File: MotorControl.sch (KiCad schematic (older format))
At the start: 3 parts, among them U4 74LVC125

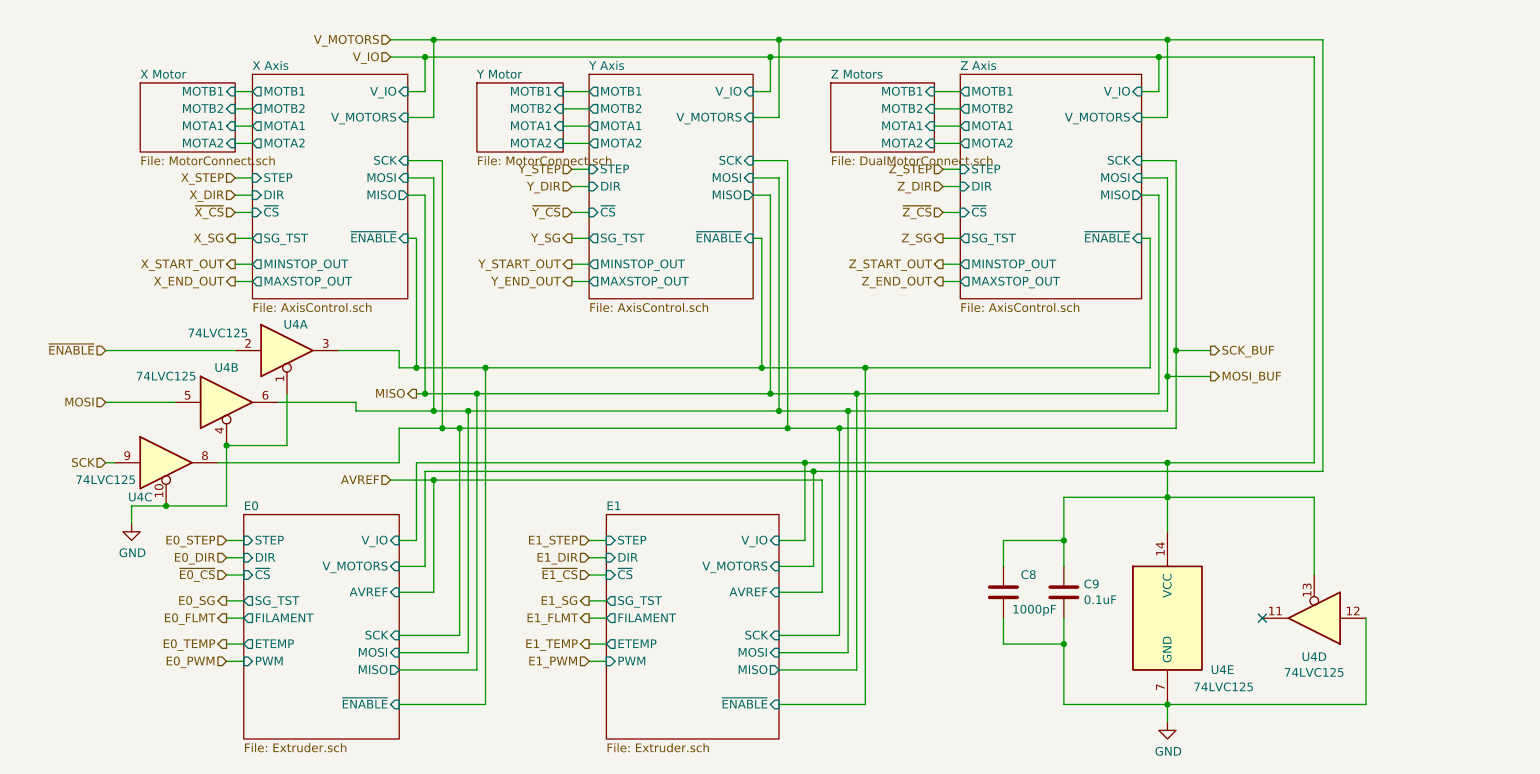
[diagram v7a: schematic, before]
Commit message: Added clock source for the TMC2660 drivers.
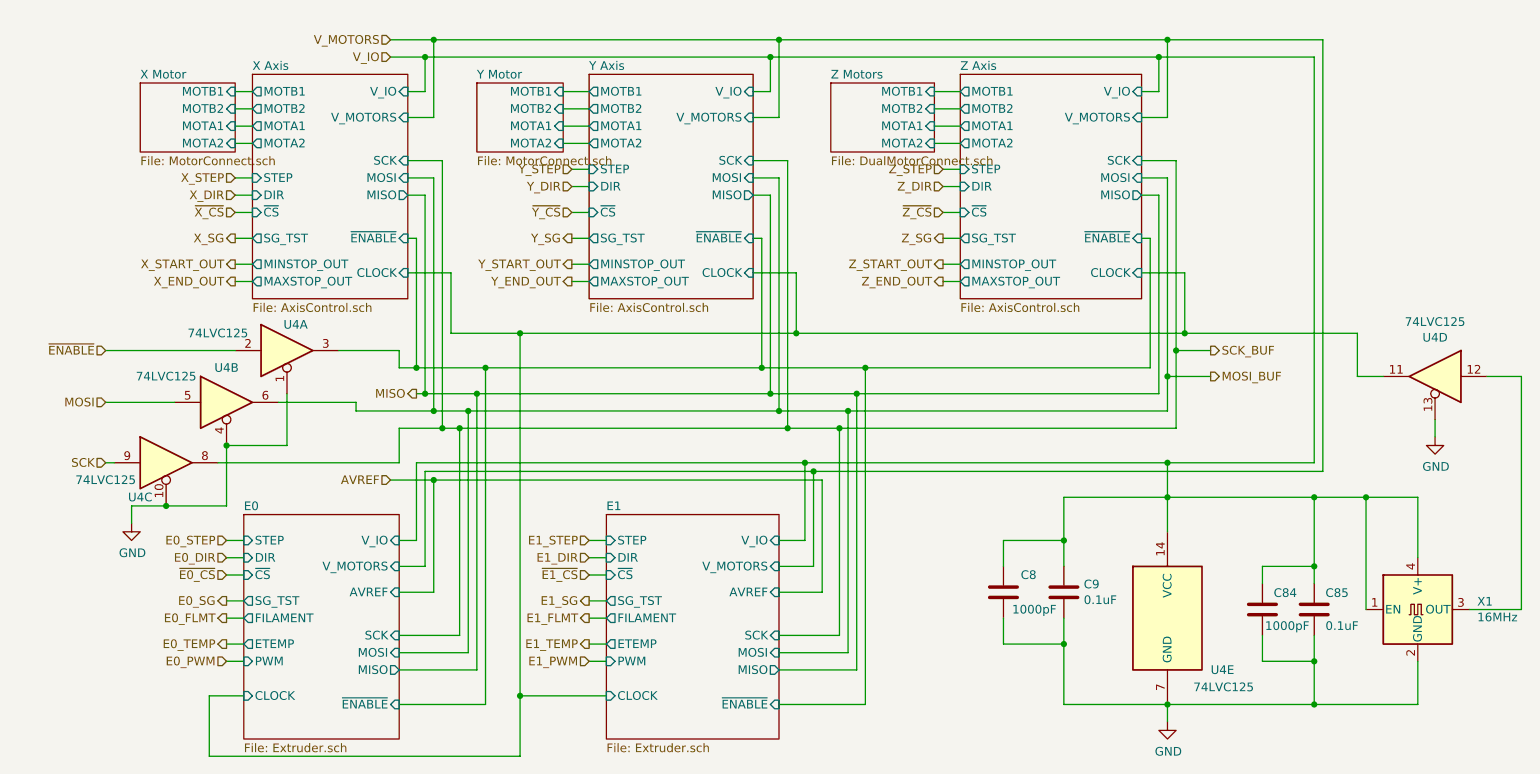
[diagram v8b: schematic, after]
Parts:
- added C84: 1000pF, PrntrBoardV1:C_0603_1608Metric, symbol Device:C
- added C85: 0.1uF, PrntrBoardV1:C_0603_1608Metric, symbol Device:C
- added X1: 16MHz, PrntrBoardV1:Oscillator_SMD_EuroQuartz_XO32-4Pin_3.2x2.5mm_HandSoldering, symbol Oscillator:XO32
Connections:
- net GND: now also U4.13, C84.2, C85.2, X1.2 (GND); no longer U4.12
- net V_IO: now also C84.1, C85.1, X1.1 (EN), X1.4 (V+); no longer U4.13
- net E0/CLOCK: now reaches U4.11
- new net: U4.12, X1.3 (OUT)
- no-connect marks 1 -> 0
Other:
- moved on the sheet: U4D
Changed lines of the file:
@@
 F14 "ETEMP" O L 3350 4600 50
 F15 "PWM" I L 3350 4700 50
+F16 "CLOCK" I L 3350 4900 50
 $EndSheet
 $Sheet
@@
 F16 "MOTA2" O L 3400 1700 50
 F17 "MOTB2" O L 3400 1500 50
+F18 "CLOCK" I R 4300 2450 50
 $EndSheet
 $Sheet
@@
 F16 "MOTA2" O L 5350 1700 50
 F17 "MOTB2" O L 5350 1500 50
+F18 "CLOCK" I R 6300 2450 50
 $EndSheet
 Wire Wire Line
@@
 F16 "MOTA2" O L 7500 1700 50
 F17 "MOTB2" O L 7500 1500 50
+F18 "CLOCK" I R 8550 2450 50
 $EndSheet
 Wire Wire Line
@@
 F14 "ETEMP" O L 5450 4600 50
 F15 "PWM" I L 5450 4700 50
+F16 "CLOCK" I L 5450 4900 50
 $EndSheet
 $Comp
 L 74ls125:74LVC125 U4
 U 4 1 5C47A3BD
-P 9550 4450
-F 0 "U4" H 9550 4675 50  0000 C CNN
-F 1 "74LVC125" H 9550 4766 50  0000 C CNN
-F 2 "Package_SO:TSSOP-14_4.4x5mm_P0.65mm" H 9550 4450 50  0001 C CNN
-F 3 "http://www.ti.com/lit/gpn/sn74LVC125" H 9550 4450 50  0001 C CNN
-	4    9550 4450
-	-1   0    0    1
-$EndComp
-Wire Wire Line
-	9850 4450 9850 4950
-Wire Wire Line
-	9850 4950 8700 4950
-Wire Wire Line
-	9550 4200 9550 3750
+P 10250 3050
+F 0 "U4" H 10250 3275 50  0000 C CNN
+F 1 "74LVC125" H 10250 3366 50  0000 C CNN
+F 2 "Package_SO:TSSOP-14_4.4x5mm_P0.65mm" H 10250 3050 50  0001 C CNN
+F 3 "http://www.ti.com/lit/gpn/sn74LVC125" H 10250 3050 50  0001 C CNN
+	4    10250 3050
+	-1   0    0    -1
+$EndComp
+$Comp
+L Oscillator:XO32 X1
+U 1 1 5CE1F94D
+P 10150 4400
+F 0 "X1" H 10494 4446 50  0000 L CNN
+F 1 "16MHz" H 10494 4355 50  0000 L CNN
+F 2 "PrntrBoardV1:Oscillator_SMD_EuroQuartz_XO32-4Pin_3.2x2.5mm_HandSoldering" H 10850 4050 50  0001 C CNN
+F 3 "http://cdn-reichelt.de/documents/datenblatt/B400/XO32.pdf" H 10050 4400 50  0001 C CNN
+	1    10150 4400
+	1    0    0    -1
+$EndComp
+$Comp
+L Device:C C85
+U 1 1 5CE20875
+P 9550 4400
+F 0 "C85" H 9615 4496 50  0000 L CNN
+F 1 "0.1uF" H 9615 4305 50  0000 L CNN
+F 2 "PrntrBoardV1:C_0603_1608Metric" H 9588 4250 50  0001 C CNN
+F 3 "~" H 9550 4400 50  0001 C CNN
+	1    9550 4400
+	1    0    0    -1
+$EndComp
+$Comp
+L Device:C C84
+U 1 1 5CE20D8C
+P 9250 4400
+F 0 "C84" H 9315 4496 50  0000 L CNN
+F 1 "1000pF" H 9265 4305 50  0000 L CNN
+F 2 "PrntrBoardV1:C_0603_1608Metric" H 9288 4250 50  0001 C CNN
+F 3 "~" H 9250 4400 50  0001 C CNN
+	1    9250 4400
+	1    0    0    -1
+$EndComp
+Wire Wire Line
+	9250 4550 9250 4700
+Wire Wire Line
+	9250 4700 9550 4700
+Wire Wire Line
+	9550 4700 9550 4950
+Wire Wire Line
+	9550 4950 8700 4950
+Wire Wire Line
+	10150 4700 10150 4950
+Wire Wire Line
+	10150 4950 9550 4950
+Connection ~ 9550 4950
+Wire Wire Line
+	9550 4550 9550 4700
+Connection ~ 9550 4700
+Wire Wire Line
+	10150 4100 10150 3750
+Wire Wire Line
+	10150 3750 9850 3750
+Wire Wire Line
+	9550 4250 9550 4150
+Connection ~ 9550 3750
 Wire Wire Line
 	9550 3750 8700 3750
-NoConn ~ 9250 4450
+Wire Wire Line
+	9250 4250 9250 4150
+Wire Wire Line
+	9250 4150 9550 4150
+Connection ~ 9550 4150
+Wire Wire Line
+	9550 4150 9550 3750
+Wire Wire Line
+	9850 4400 9850 3750
+Connection ~ 9850 3750
+Wire Wire Line
+	9850 3750 9550 3750
+Wire Wire Line
+	10750 4400 10750 3050
+Wire Wire Line
+	10750 3050 10550 3050
+$Comp
+L power:GND #PWR088
+U 1 1 5CE2301E
+P 10250 3400
+F 0 "#PWR088" H 10250 3150 50  0001 C CNN
+F 1 "GND" H 10255 3227 50  0000 C CNN
+F 2 "" H 10250 3400 50  0001 C CNN
+F 3 "" H 10250 3400 50  0001 C CNN
+	1    10250 3400
+	1    0    0    -1
+$EndComp
+Wire Wire Line
+	10250 3300 10250 3400
+Wire Wire Line
+	4300 2450 4550 2450
+Wire Wire Line
+	4550 2450 4550 2800
+Wire Wire Line
+	4550 2800 4950 2800
+Wire Wire Line
+	9800 2800 9800 3050
+Wire Wire Line
+	9800 3050 9950 3050
+Wire Wire Line
+	8550 2450 8800 2450
+Wire Wire Line
+	8800 2450 8800 2800
+Connection ~ 8800 2800
+Wire Wire Line
+	8800 2800 9800 2800
+Wire Wire Line
+	6300 2450 6550 2450
+Wire Wire Line
+	6550 2450 6550 2800
+Connection ~ 6550 2800
+Wire Wire Line
+	6550 2800 8800 2800
+Wire Wire Line
+	5450 4900 4950 4900
+Wire Wire Line
+	4950 4900 4950 2800
+Connection ~ 4950 2800
+Wire Wire Line
+	4950 2800 6550 2800
+Wire Wire Line
+	3350 4900 3150 4900
+Wire Wire Line
+	3150 4900 3150 5250
+Wire Wire Line
+	3150 5250 4950 5250
+Wire Wire Line
+	4950 5250 4950 4900
+Connection ~ 4950 4900
+Wire Wire Line
+	10450 4400 10750 4400
 $EndSCHEMATC
